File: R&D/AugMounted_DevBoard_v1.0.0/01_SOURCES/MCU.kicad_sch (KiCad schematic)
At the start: 20 parts, among them J201 J_TYPE-C-31-M-13, U202 U_MCP23017T-E/ML

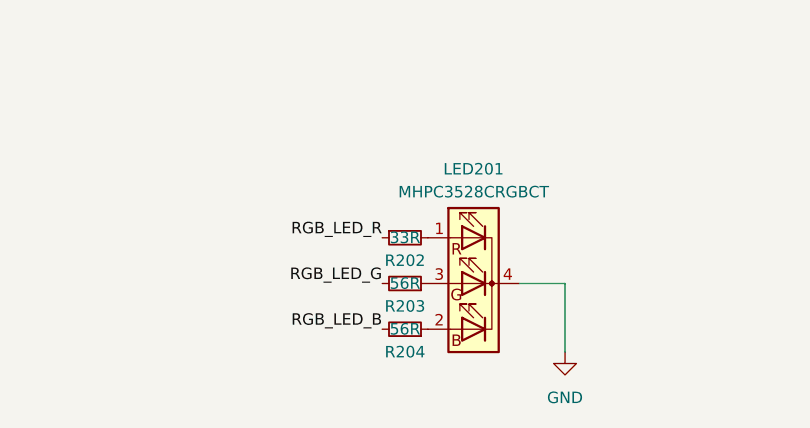
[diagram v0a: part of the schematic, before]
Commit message: Changed layout + all passive to 0402
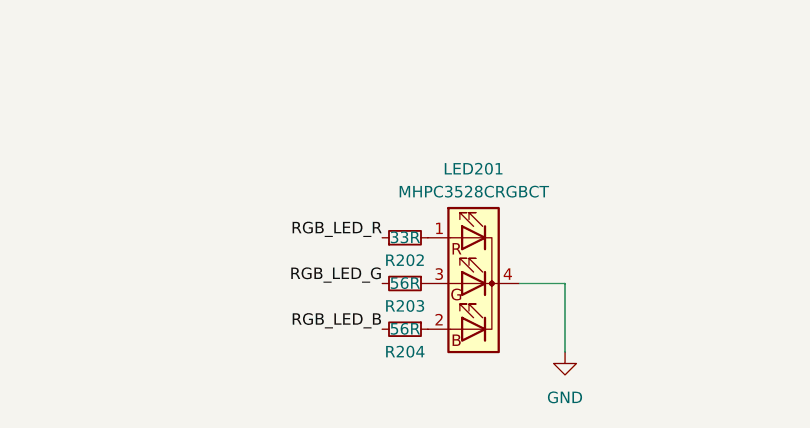
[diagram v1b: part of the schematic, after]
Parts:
- removed R202: R_0603_33R_1%_0.1W, .mounted-lib:R_0603_1608Metric, symbol .mounted-lib:R_0603_33R_1%_0.1W
- removed R203, R204: R_0603_56R_1%_0.1W, .mounted-lib:R_0603_1608Metric, symbol .mounted-lib:R_0603_56R_1%_0.1W
- added R202: R_0402_33R_1%_0.06W, .mounted-lib:R_0402_1005Metric, symbol .mounted-lib:R_0402_33R_1%_0.06W
- added R203, R204: R_0402_56R_1%_0.06W, .mounted-lib:R_0402_1005Metric, symbol .mounted-lib:R_0402_56R_1%_0.06W
- C201: value C_0603_1uF_16V_X7R_10% -> C_0402_1uF_10V_X7R_10%; footprint .mounted-lib:C_0603_1608Metric -> .mounted-lib:C_0402_1005Metric; symbol .mounted-lib:C_0603_1uF_16V_X7R_10%_1 -> .mounted-lib:C_0402_1uF_10V_X7R_10%; MaxHeight_mm 0.8mm -> 0.5mm; Package C0603 -> C0402; Voltage 16V -> 10V
- C203, C204: footprint .mounted-lib:C_0603_1608Metric -> .mounted-lib:C_0402_1005Metric; symbol .mounted-lib:C_0603_100nF_100V_X7R_10% -> .mounted-lib:C_0402_100nF_50V_X7R_10%; MaxHeight_mm 0.8mm -> 0.5mm; Voltage 100V -> 50V
- R201: footprint .mounted-lib:R_0603_1608Metric -> .mounted-lib:R_0402_1005Metric; symbol .mounted-lib:R_0603_10k_1%_0.1W -> .mounted-lib:R_0402_10k_1%_0.06W; MaxHeight_mm 0.55mm -> 0.35mm; Package R0603 -> R0402; Power_W 0.1W -> 0.06W
- R205, R206: footprint .mounted-lib:R_0603_1608Metric -> .mounted-lib:R_0402_1005Metric; symbol .mounted-lib:R_0603_4.7k_1%_0.1W -> .mounted-lib:R_0402_4.7k_1%_0.06W; MaxHeight_mm 0.55mm -> 0.35mm; Package R0603 -> R0402; Power_W 0.1W -> 0.06W
- R207, R208: footprint .mounted-lib:R_0603_1608Metric -> .mounted-lib:R_0402_1005Metric; symbol .mounted-lib:R_0603_5.23k_1%_0.1W -> .mounted-lib:R_0402_5.23k_1%_0.06W; MaxHeight_mm 0.55mm -> 0.35mm; Package R0603 -> R0402; Power_W 0.1W -> 0.06W
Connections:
- net RGB_LED_B: now also R204.2
- net RGB_LED_G: now also R203.2
- net RGB_LED_R: now also R202.1
- net at LED201.1 (RA): now also R202.2
- net at LED201.2 (GA): now also R204.1
- net at LED201.3 (BA): now also R203.1

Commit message: Component layout is done, routing video signals is done too.
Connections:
- net B1: now also U?.21 (GPIO13/TOUCH13/ADC2_CH2/FSPIQ/FSPIIO7/SUBSPIQ); no longer U?.22 (GPIO14/TOUCH14/ADC2_CH3/FSPIWP/FSPIDQS/SUBSPIWP)
- net B2: now also U?.22 (GPIO14/TOUCH14/ADC2_CH3/FSPIWP/FSPIDQS/SUBSPIWP); no longer U?.21 (GPIO13/TOUCH13/ADC2_CH2/FSPIQ/FSPIIO7/SUBSPIQ)
- net B3: now also U?.26 (GPIO45); no longer U?.20 (GPIO12/TOUCH12/ADC2_CH1/FSPICLK/FSPIIO6/SUBSPICLK)
- net B4: now also U?.24 (GPIO47/SPICLK_P/SUBSPICLK_P_DIFF); no longer U?.19 (GPIO11/TOUCH11/ADC2_CH0/FSPID/FSPIIO5/SUBSPID)
- net B5: now also U?.25 (GPIO48/SPICLK_N/SUBSPICLK_N_DIFF); no longer U?.18 (GPIO10/TOUCH10/ADC1_CH9/FSPICS0/FSPIIO4/SUBSPICS0)
- net G3: now also U?.20 (GPIO12/TOUCH12/ADC2_CH1/FSPICLK/FSPIIO6/SUBSPICLK); no longer U?.26 (GPIO45)
- net G4: now also U?.18 (GPIO10/TOUCH10/ADC1_CH9/FSPICS0/FSPIIO4/SUBSPICS0); no longer U?.25 (GPIO48/SPICLK_N/SUBSPICLK_N_DIFF)
- net G5: now also U?.19 (GPIO11/TOUCH11/ADC2_CH0/FSPID/FSPIIO5/SUBSPID); no longer U?.24 (GPIO47/SPICLK_P/SUBSPICLK_P_DIFF)
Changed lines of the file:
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@@
     (effects (font (size 1.27 1.27)) (justify left))
   )
-  (hierarchical_label "B2" (shape bidirectional) (at 139.7 83.82 0) (fields_autoplaced)
+  (hierarchical_label "B2" (shape bidirectional) (at 139.7 86.36 0) (fields_autoplaced)
     (effects (font (size 1.27 1.27)) (justify left))
   )
-  (hierarchical_label "B3" (shape bidirectional) (at 139.7 81.28 0) (fields_autoplaced)
+  (hierarchical_label "B3" (shape bidirectional) (at 139.7 99.06 0) (fields_autoplaced)
     (effects (font (size 1.27 1.27)) (justify left))
   )
@@
     (effects (font (size 1.27 1.27)) (justify left))
   )
-  (hierarchical_label "G4" (shape bidirectional) (at 139.7 106.68 0) (fields_autoplaced)
+  (hierarchical_label "G4" (shape bidirectional) (at 139.7 76.2 0) (fields_autoplaced)
     (effects (font (size 1.27 1.27)) (justify left))
   )
-  (hierarchical_label "B1" (shape bidirectional) (at 139.7 86.36 0) (fields_autoplaced)
+  (hierarchical_label "B1" (shape bidirectional) (at 139.7 83.82 0) (fields_autoplaced)
     (effects (font (size 1.27 1.27)) (justify left))
   )
@@
     (effects (font (size 1.27 1.27)) (justify right))
   )
-  (hierarchical_label "G5" (shape bidirectional) (at 139.7 104.14 0) (fields_autoplaced)
+  (hierarchical_label "G5" (shape bidirectional) (at 139.7 78.74 0) (fields_autoplaced)
     (effects (font (size 1.27 1.27)) (justify left))
   )
@@
     (effects (font (size 1.27 1.27)) (justify left))
   )
-  (hierarchical_label "G3" (shape bidirectional) (at 139.7 99.06 0) (fields_autoplaced)
+  (hierarchical_label "G3" (shape bidirectional) (at 139.7 81.28 0) (fields_autoplaced)
     (effects (font (size 1.27 1.27)) (justify left))
   )
@@
     (effects (font (size 1.27 1.27)) (justify left))
   )
-  (hierarchical_label "B5" (shape bidirectional) (at 139.7 76.2 0) (fields_autoplaced)
+  (hierarchical_label "B5" (shape bidirectional) (at 139.7 106.68 0) (fields_autoplaced)
     (effects (font (size 1.27 1.27)) (justify left))
   )
@@
     (effects (font (size 1.27 1.27)) (justify left))
   )
-  (hierarchical_label "B4" (shape bidirectional) (at 139.7 78.74 0) (fields_autoplaced)
+  (hierarchical_label "B4" (shape bidirectional) (at 139.7 104.14 0) (fields_autoplaced)
     (effects (font (size 1.27 1.27)) (justify left))
   )

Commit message: Layout almost done
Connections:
- net CC1: now also D201.6 (IO4); no longer D201.4 (IO3)
- net CC2: now also D201.4 (IO3); no longer D201.6 (IO4)
- net USB_D+: now also D201.3 (IO2); no longer D201.1 (IO1)
- net USB_D-: now also D201.1 (IO1); no longer D201.3 (IO2)
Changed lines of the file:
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@@
     (stroke (width 0) (type default))
   )
-  (label "CC1" (at 273.05 45.72 0) (fields_autoplaced)
+  (label "CC1" (at 273.05 50.8 0) (fields_autoplaced)
     (effects (font (size 1.27 1.27)) (justify left bottom))
   )
@@
     (effects (font (size 1.27 1.27)) (justify right bottom))
   )
-  (label "CC2" (at 273.05 50.8 0) (fields_autoplaced)
+  (label "CC2" (at 273.05 45.72 0) (fields_autoplaced)
     (effects (font (size 1.27 1.27)) (justify left bottom))
   )
@@
     (effects (font (size 1.27 1.27)) (justify left bottom))
   )
-  (label "USB_D+" (at 247.65 45.72 180) (fields_autoplaced)
+  (label "USB_D+" (at 247.65 50.8 180) (fields_autoplaced)
     (effects (font (size 1.27 1.27)) (justify right bottom))
   )
@@
     (effects (font (size 1.27 1.27)) (justify left bottom))
   )
-  (label "USB_D-" (at 247.65 50.8 180) (fields_autoplaced)
+  (label "USB_D-" (at 247.65 45.72 180) (fields_autoplaced)
     (effects (font (size 1.27 1.27)) (justify right bottom))
   )
